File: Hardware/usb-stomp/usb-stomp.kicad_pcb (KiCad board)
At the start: 4 copper layers, 100 x 50 mm, 130 parts, among them J101 USB_C_Receptacle_USB2.0_16P, J102 Barrel_Jack_Switch, J103 AudioJack3_SwitchTR, J201 AudioJack4, J202 AudioJack4, J301 AudioJack3_SwitchTR, J302 AudioJack3_SwitchTR, SW101 SW_SPST, SW102 RotaryEncoder_Switch_MP, U101 USBLC6-2P6, U102 M24C64-FMH6TG, U103 TPS62153, U104 TLV76733DRVx, U201 SN74AHCT1G125DCKR, U202 TLP2310, U301 OPA2365AIDR, U302 TLV76733DRVx, U303 TAC5242, U401 RP2354A, Y401 ABM8-272-T3

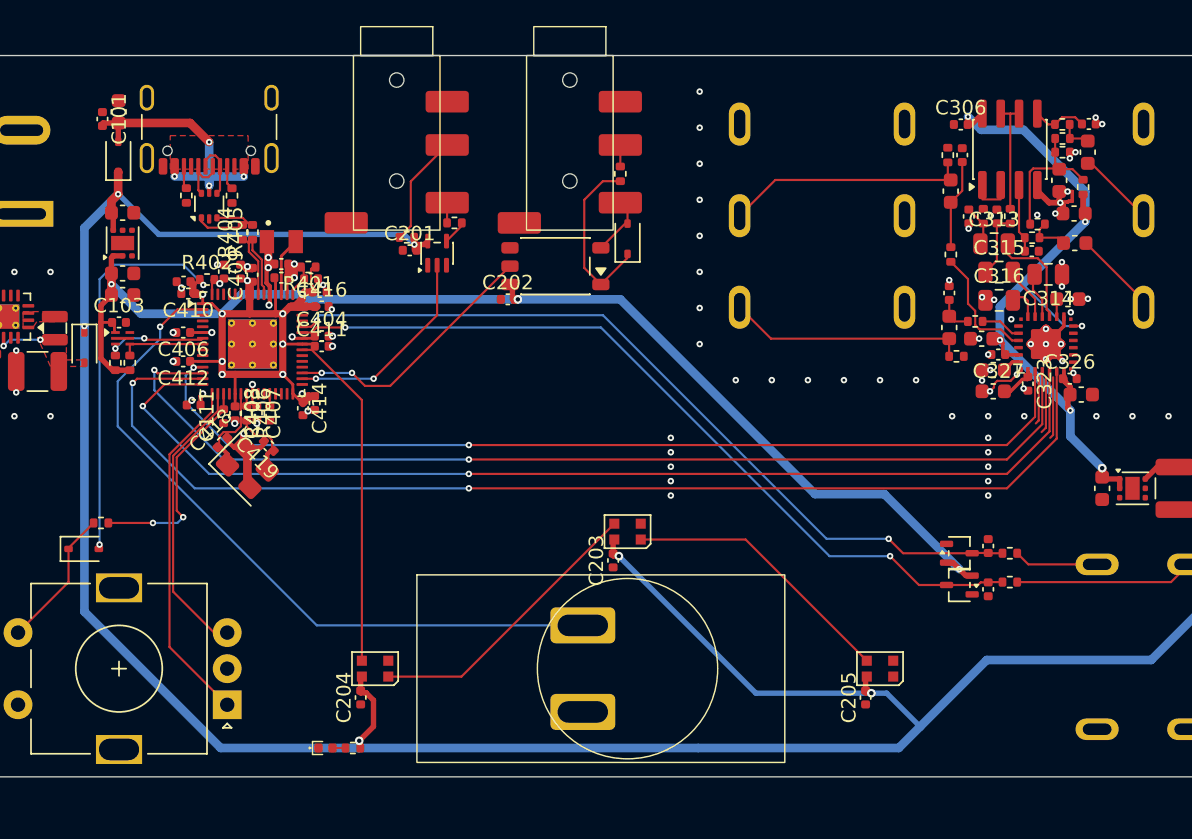
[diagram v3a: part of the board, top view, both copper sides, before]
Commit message: Commit PCB state after initial fixup of 0201 -> 0402 size change
This is a quick first run of fixing up the change to 0402 components.
It's DRC-clean but still needs checking that I also did things like move
the ground vias out of the paste layer etc.

Also the incidental fixing of all the through-hole components: they
should have thermal relief spokes to make soldering them easier.

Signed-off-by: Linus Torvalds <torvalds@linux-foundation.org>
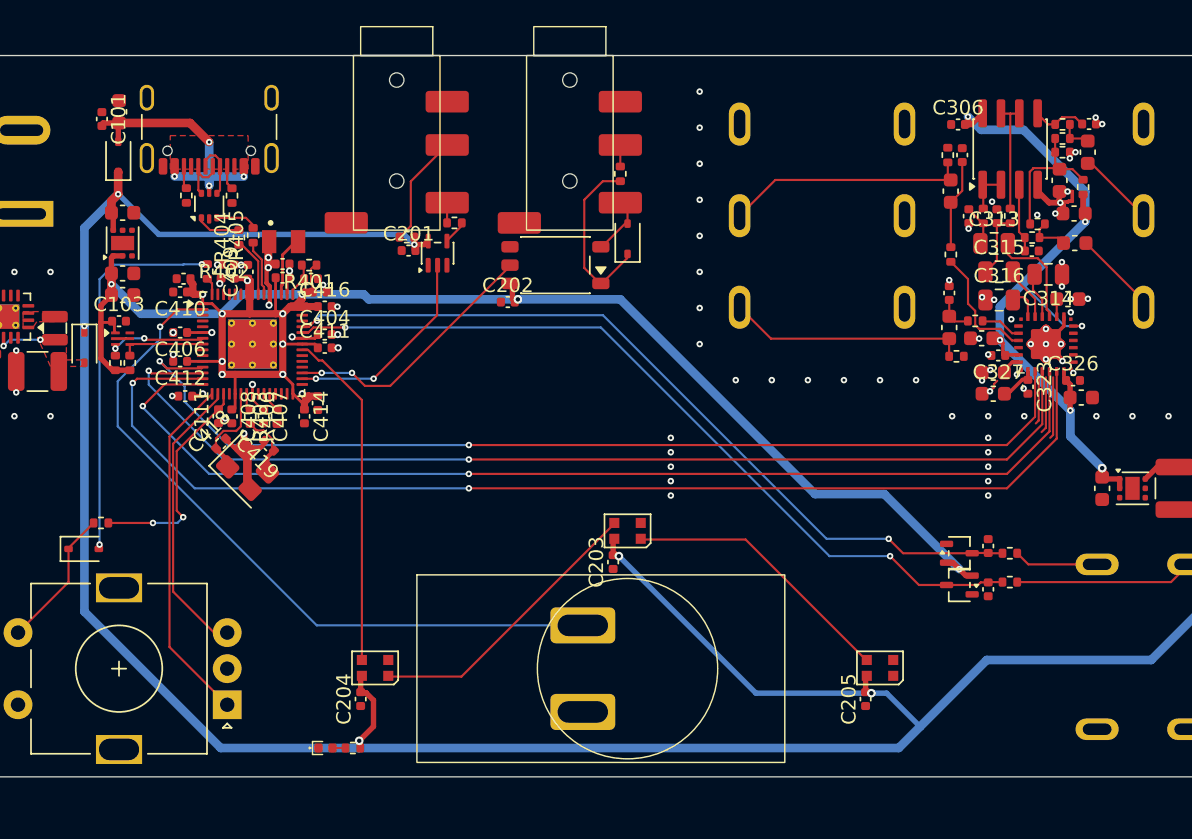
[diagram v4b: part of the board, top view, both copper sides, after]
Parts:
- moved C420 0.85 mm to (69.3, 93.6)
- moved C410 0.57 mm to (69.0, 86.4)
- moved C414 0.57 mm to (77.6, 95.0)
- moved R403 0.56 mm to (75.7, 95.0)
- moved R402 0.56 mm to (70.9, 85.0), turned to -90 degrees
- moved C407 0.52 mm to (74.8, 95.0)
- moved R404 0.43 mm to (73.1, 82.6)
- moved C413 0.43 mm to (72.7, 85.0)
- moved C409 0.39 mm to (73.7, 85.0)
- moved C111 0.36 mm to (71.6, 95.0)
- moved R406 0.34 mm to (73.8, 95.0)
- moved C408 0.31 mm to (72.6, 95.0)
- moved C326 0.26 mm to (130.9, 92.5)
- moved C404 0.24 mm to (79.0, 89.3)
- moved C411 0.24 mm to (79.0, 90.3)
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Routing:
- net GND: track 47.1 -> 42.3 mm, vias 98 -> 94
- net /RP2354/GPIO8: track 67.4 -> 70.9 mm
- net +3V3: track 155.2 -> 157.0 mm
- net Net-(U301A--): track 1.27 -> 2.94 mm
- net /BOOTSEL: track 27.3 -> 26.2 mm
- net Net-(C419-Pad1): track 4.94 -> 4.22 mm

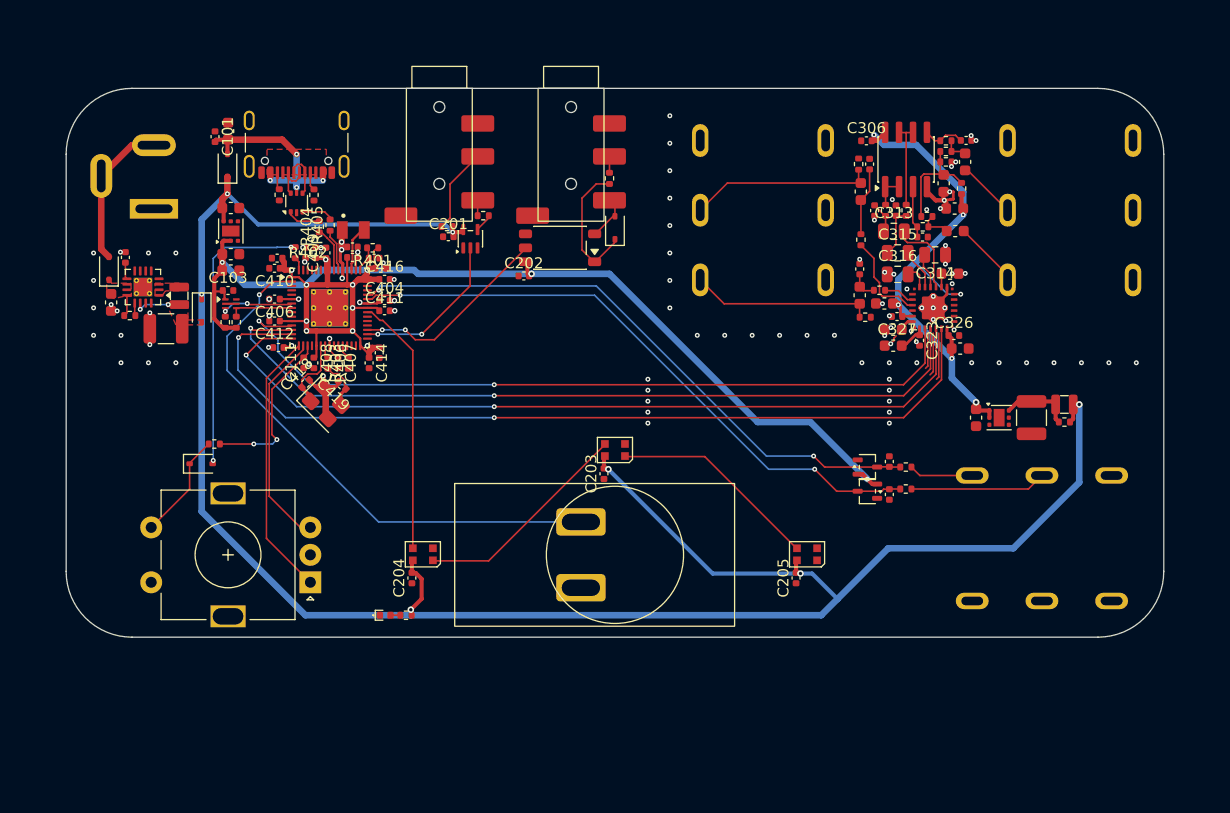
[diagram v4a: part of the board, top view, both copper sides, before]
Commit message: Update usb-stomp board layout
Let's make it slightly less wide - move the MIDI connectors to
the left side to make room, and put the rotary at the top instead
where you won't stomp on it by mistake.

Make the board a bit taller instead, and switch to the side-lit
WS2812B-4020 LEDs at the bottom. Add a couple more, just in case:
once you have one, the rest are basically "free".

The through-hole components are now marked for thermal relief to
make them easier to solder.

And the eeprom is now gone for good, since I ended up just using a
portion of the rp2354 flash to save scene state in the end.

Signed-off-by: Linus Torvalds <torvalds@linux-foundation.org>
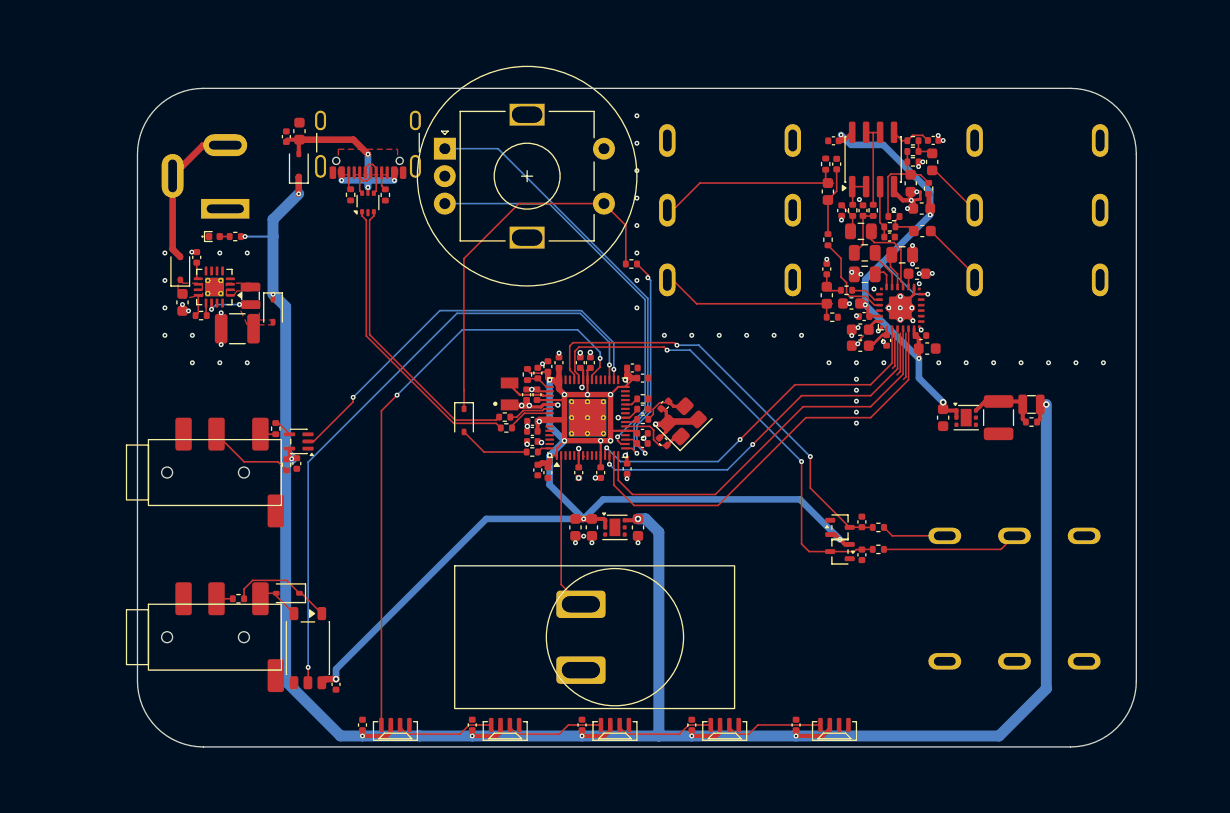
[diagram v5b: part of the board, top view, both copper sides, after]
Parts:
- removed the C103 at (64.8, 88.4)
- removed the R104 at (64.5, 91.3)
- removed the R105 at (65.5, 91.3)
- removed the U102 at (65.0, 89.6)
- added C206: 0.1uF, Capacitor_SMD:C_0402_1005Metric, F.Cu at (107.0, 128.0)
- added C207: 0.1uF, Capacitor_SMD:C_0402_1005Metric, F.Cu at (116.5, 128.0)
- added D205: WS2812B-4020, Mylib:WS2812B-4020, F.Cu at (110.0, 128.0)
- added D206: WS2812B-4020, Mylib:WS2812B-4020, F.Cu at (120.0, 128.0)
- D202, D203, D204: value WS2812B-2020-V6 -> WS2812B-4020; footprint LED_SMD:LED_WS2812B-2020_PLCC4_2.0x2.0mm -> Mylib:WS2812B-4020
- moved J201 63.1 mm to (57.5, 120.0), turned to 0 degrees
- moved R201 51.1 mm to (65.7, 116.5), turned to 0 degrees
- moved C108 47.2 mm to (102.1, 110.0), turned to -90 degrees
- moved D201 44.7 mm to (70.2, 116.0), turned to 180 degrees
- moved U103 44.2 mm to (100.0, 110.0), turned to 0 degrees
- moved J202 43.9 mm to (57.5, 105.0), turned to 0 degrees
- moved U202 43.1 mm to (72.0, 121.0), turned to -90 degrees
- moved R107 41.4 mm to (101.5, 86.0)
- moved SW102 41.4 mm to (84.5, 75.5), turned to 0 degrees
- moved C111 41.3 mm to (97.9, 110.0), turned to -90 degrees
- moved C202 41.0 mm to (74.6, 124.3), turned to 90 degrees
- moved C109 39.2 mm to (96.4, 110.0), turned to -90 degrees
- moved D102 37.8 mm to (63.5, 83.5)
- moved R103 37.8 mm to (65.4, 83.5)
- moved C420 33.6 mm to (101.1, 104.7), turned to -90 degrees
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- renumbered C104 to C103, C105 to C104, C106 to C105, C107 to C106, C108 to C107, C109 to C108, C110 to C109, C111 to C110, C112 to C111, R106 to R104, R107 to R105, R108 to R106, R109 to R107, U103 to U102, U104 to U103
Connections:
- net /RP2354/GPIO10 renamed /TAC5242/I2S.DIN
- net /RP2354/GPIO11 renamed /TAC5242/I2S.DOUT
- net /RP2354/GPIO8 renamed /TAC5242/I2S.BCLK
- net /RP2354/GPIO9 renamed /TAC5242/I2S.FSYNC
- D202 pad 1: Net-(D202-DOUT) -> /RP2354/GPIO25
- D202 pad 2: GND -> +5V
- D202 pad 3: /RP2354/GPIO25 -> Net-(D202-DOUT)
- D202 pad 4: +5V -> GND
- D203 pad 1: Net-(D203-DOUT) -> Net-(D202-DOUT)
- D203 pad 2: GND -> +5V
- D203 pad 3: Net-(D202-DOUT) -> Net-(D203-DOUT)
- D203 pad 4: +5V -> GND
- D204 pad 1: unconnected-(D204-DOUT-Pad1) -> Net-(D203-DOUT)
- D204 pad 2: GND -> +5V
- D204 pad 3: Net-(D203-DOUT) -> Net-(D204-DOUT)
- D204 pad 4: +5V -> GND
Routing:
- net /TAC5242/I2S.DIN: track 79.9 -> 39.7 mm, vias 2 -> 0
- net /RP2354/GPIO21: track 18.2 -> 57.7 mm
- net /TAC5242/I2S.FSYNC: track 73.5 -> 34.8 mm
- net /TAC5242/I2S.DOUT: track 75.0 -> 37.4 mm, vias 2 -> 0
- net /TAC5242/I2S.BCLK: track 70.9 -> 34.1 mm
- net /RP2354/GPIO0: track 49.5 -> 14.3 mm, vias 1 -> 0
- net /RP2354/GPIO25: track 23.6 -> 55.3 mm, vias 0 -> 2
- net Net-(D106-K): track 9.77 -> 34.9 mm
- net /USB-D+: track 3.10 -> 27.2 mm
- net /USB-D-: track 2.92 -> 26.7 mm
- net /RP2354/GPIO20: track 14.6 -> 37.6 mm
- net /BOOTSEL: track 26.2 -> 6.46 mm, vias 2 -> 0
- net /RP2354/GPIO13: track 19.9 -> 36.6 mm, vias 0 -> 1
- net /RP2354/ADC1: track 55.8 -> 39.7 mm
- net /RP2354/GPIO12: track 24.4 -> 40.1 mm, vias 0 -> 1
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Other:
- board size 100 x 50 mm -> 91 x 60 mm

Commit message: Update usb-stomp board with new-and-improved TAC5242 footprint
This fixes up the TAC5242 use and removes the now unnecessary manual
vias and traces, but does not actually do the shuffling of components,
so the bigger courtyard of the TAC5242 now makes DRC complain about
footprint overlaps as expected.

Actually shuffling components around comes next.

Signed-off-by: Linus Torvalds <torvalds@linux-foundation.org>
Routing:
- net GND: track 42.9 -> 29.5 mm, vias 93 -> 86

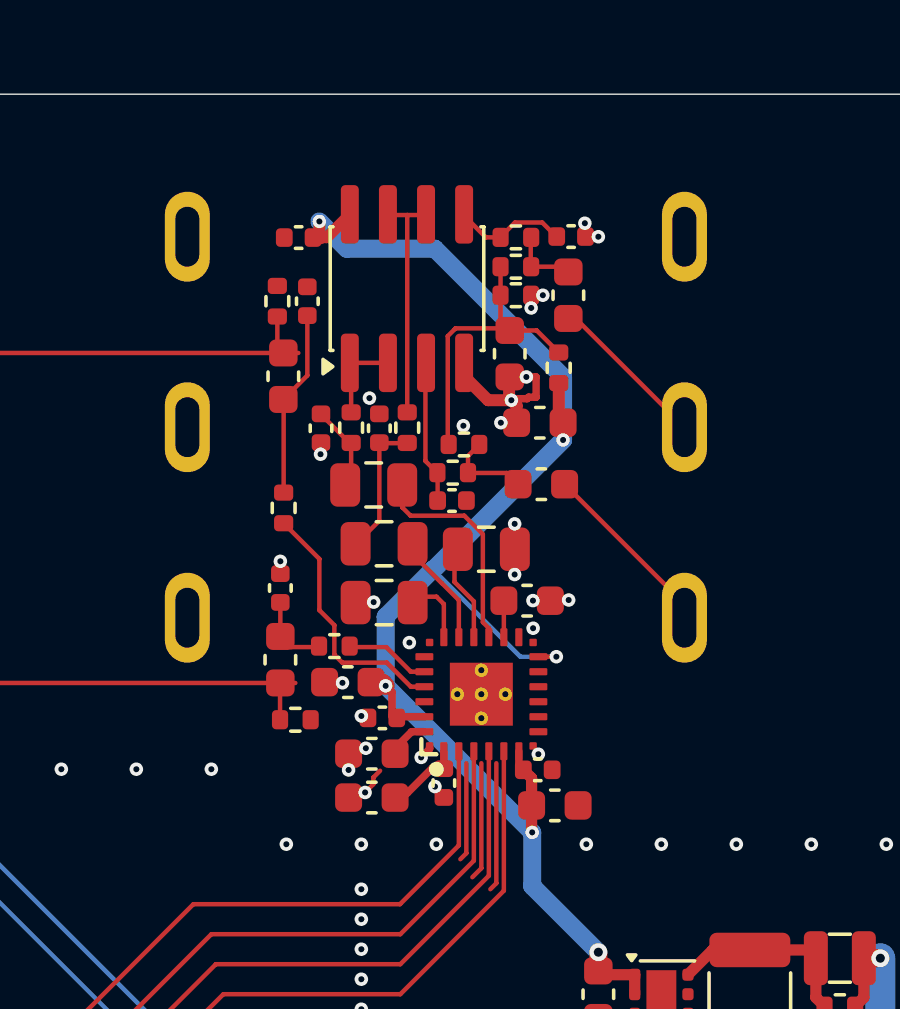
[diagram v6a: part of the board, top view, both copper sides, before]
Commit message: Clear up the TAC5242 courtyard overlaps
This is me trying to do board cleanups like the TAC5242 courtyard
updates using some automated tooling with Opus instead of moving things
by hand.  I don't think it actually makes for less work that it would
have been to just do things by hand, but the hope is that maybe it will
pay off in the long run.

The tooling itself is not nearly ready to be public, so this is just the
end result of some tool-assisted "wiggle parts around so that they fit"
with Opus driving that.

Signed-off-by: Linus Torvalds <torvalds@linux-foundation.org>
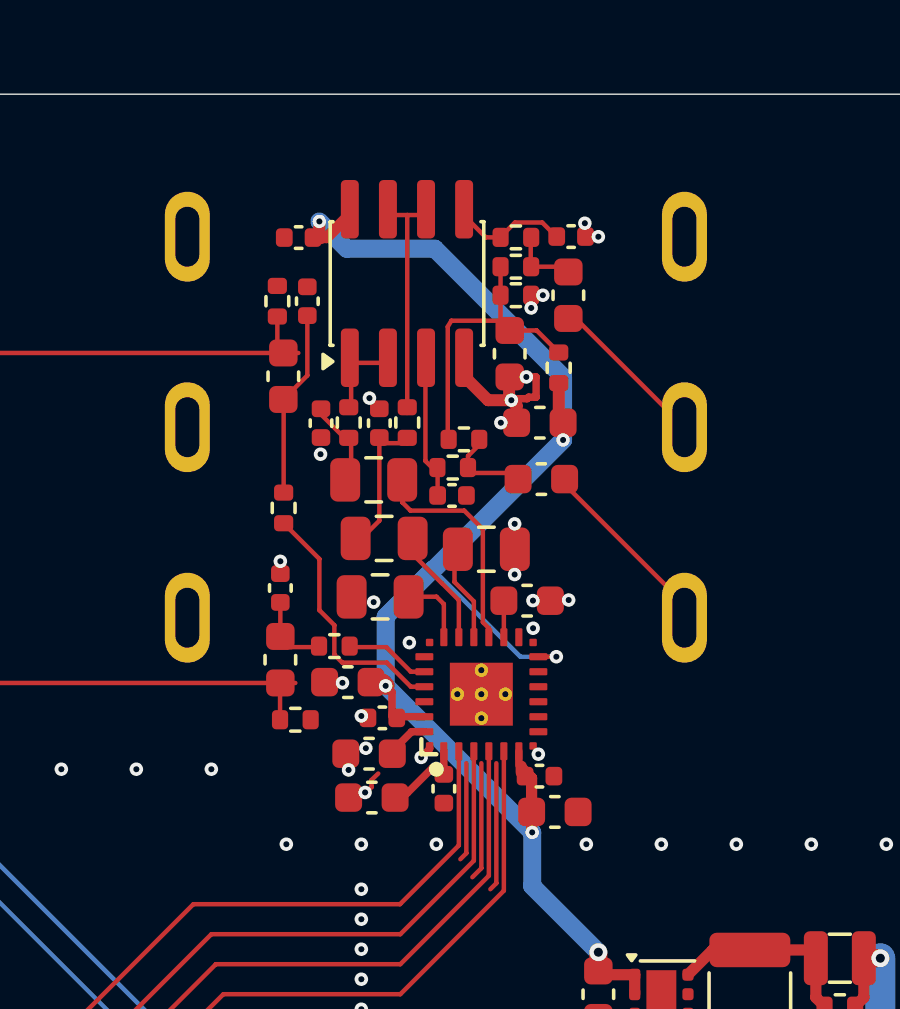
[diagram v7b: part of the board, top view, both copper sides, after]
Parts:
- moved C316 0.23 mm to (122.6, 86.8)
- moved C326 0.22 mm to (127.9, 92.7)
- moved C319 0.22 mm to (128.4, 93.9)
- moved C323 0.19 mm to (124.8, 93.2)
- moved R311 0.19 mm to (121.6, 80.9)
- moved C315 0.18 mm to (122.8, 84.8)
- moved C302 0.17 mm to (128.0, 82.8)
- moved C307 0.17 mm to (125.0, 83.4)
- moved C311 0.17 mm to (120.7, 81.0)
- moved C312 0.17 mm to (122.6, 81.0)
- moved C313 0.17 mm to (122.4, 82.9)
- moved R304 0.17 mm to (125.4, 81.5)
- moved R307 0.17 mm to (125.0, 82.4)
- moved R312 0.17 mm to (123.5, 80.9)
- moved U301 0.17 mm to (123.5, 76.3)
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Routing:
- net GND: track 29.5 -> 29.4 mm, vias 86 -> 84
